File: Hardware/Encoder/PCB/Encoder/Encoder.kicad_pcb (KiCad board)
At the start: 2 copper layers, 20.3 x 40.6 mm, 2 parts, among them J1 Conn_01x06_Male, SW1 RotaryEncoder_Switch

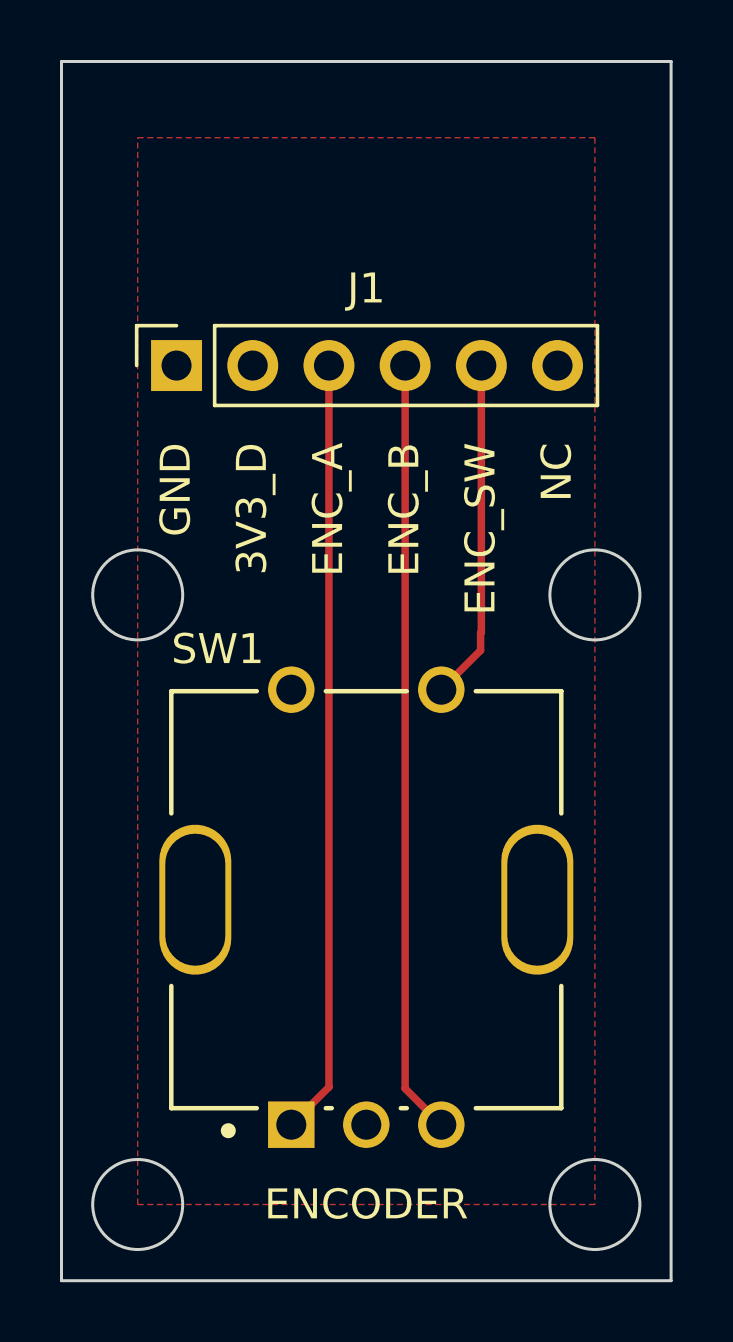
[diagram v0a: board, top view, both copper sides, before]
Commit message: Removing edge and mount holes
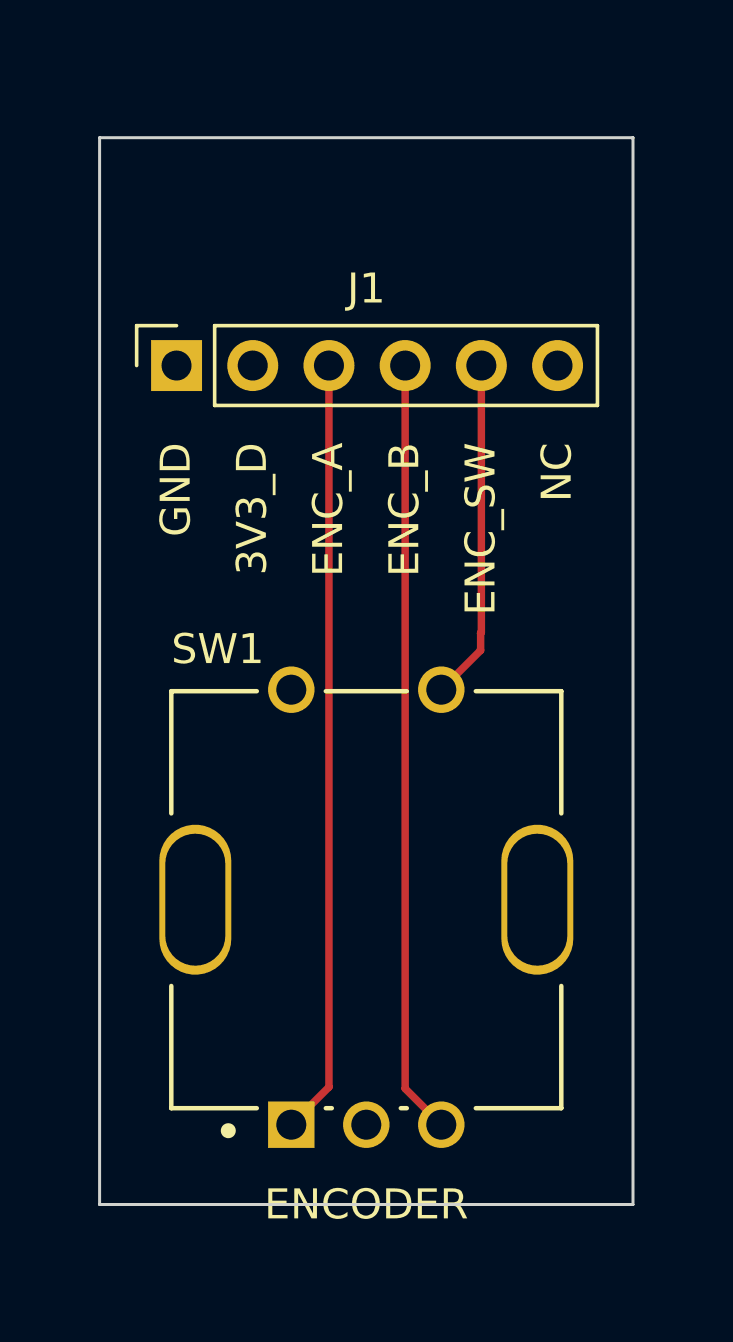
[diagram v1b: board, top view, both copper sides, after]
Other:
- board size 20.3 x 40.6 mm -> 17.8 x 35.6 mm

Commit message: Finalised PCBs
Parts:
- J1: footprint Connector_PinSocket_2.54mm:PinSocket_1x06_P2.54mm_Vertical -> Connector_PinHeader_2.54mm:PinHeader_1x06_P2.54mm_Horizontal
- moved J1 2.56 mm to (92.7, 63.5)
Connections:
- SW1 pad 1: GND -> (no net)
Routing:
- net ENC_SW: track 11.3 -> 8.79 mm
- net ENC_B: track 25.8 -> 23.2 mm
- net ENC_A: track 25.8 -> 23.3 mm
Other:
- board size 17.8 x 35.6 mm -> 17.8 x 29.8 mm
- board text added: "A"
- board text added: "B"
- board text added: "SW"
- board text removed: "ENC_A"
- board text removed: "ENC_B"
- board text removed: "ENC_SW"
